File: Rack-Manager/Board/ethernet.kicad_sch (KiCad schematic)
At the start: 2 parts, among them J1 ARJM11C7-114-BA-EW2, U7 W6100Q

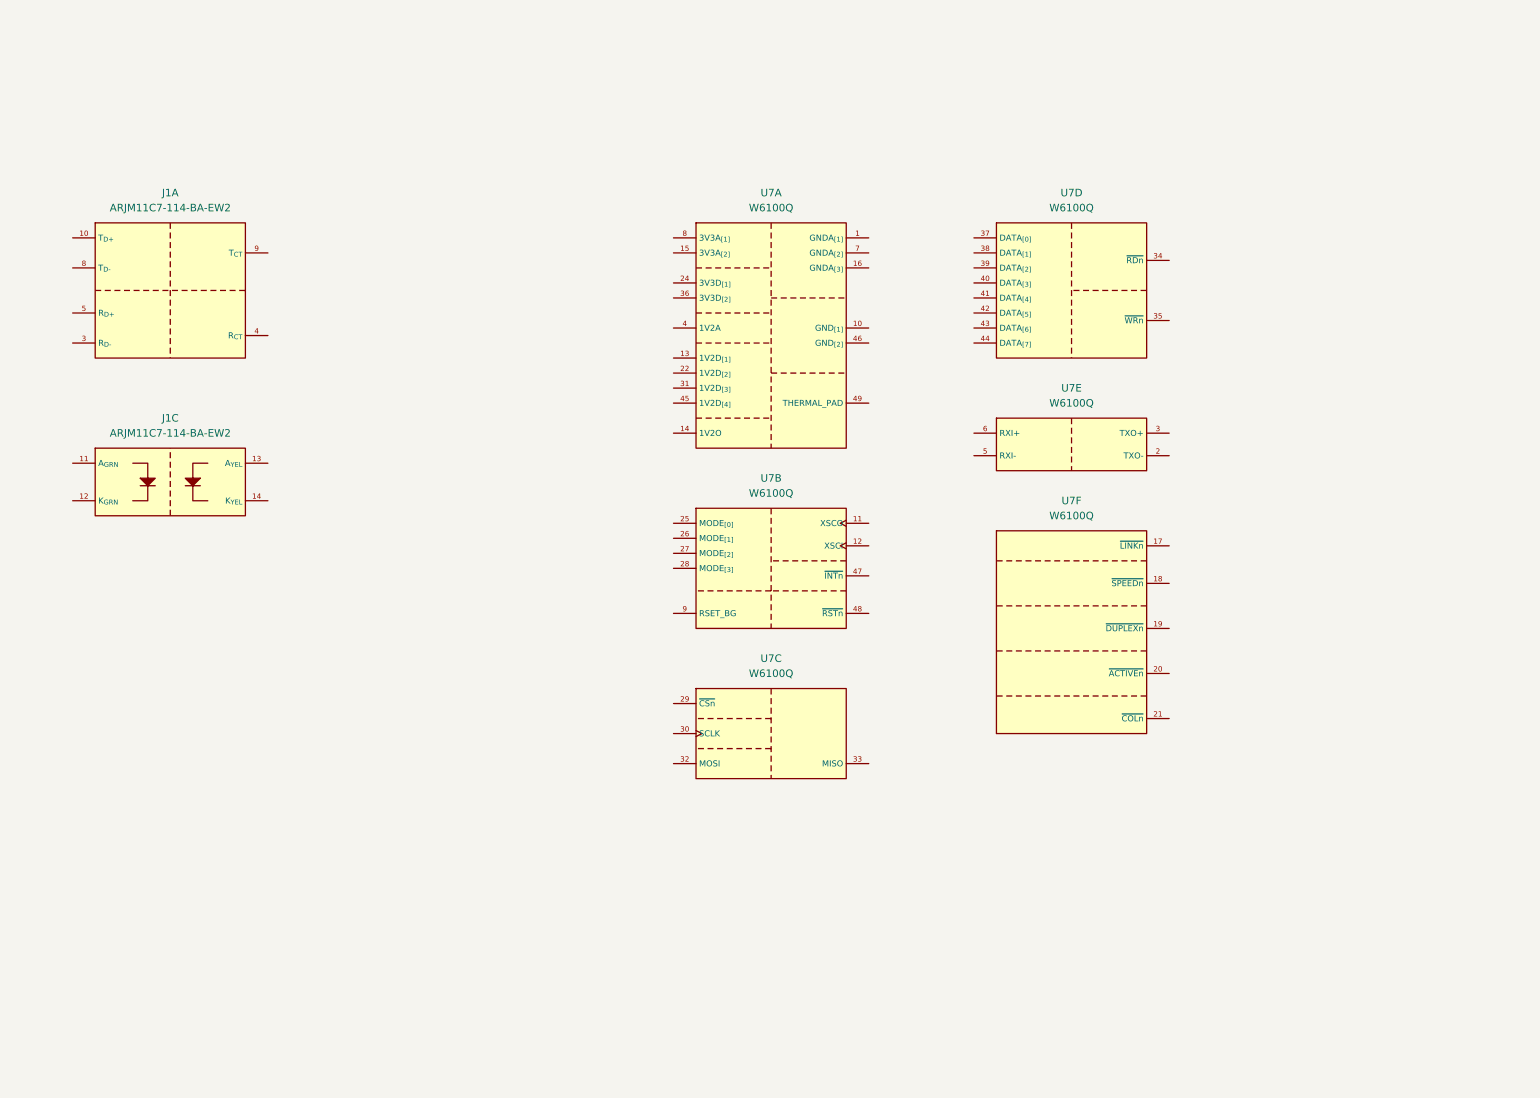
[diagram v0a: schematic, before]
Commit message: Updated Texas Instruments and WIZnet KiCAD libraries. Continued with the schematics design.
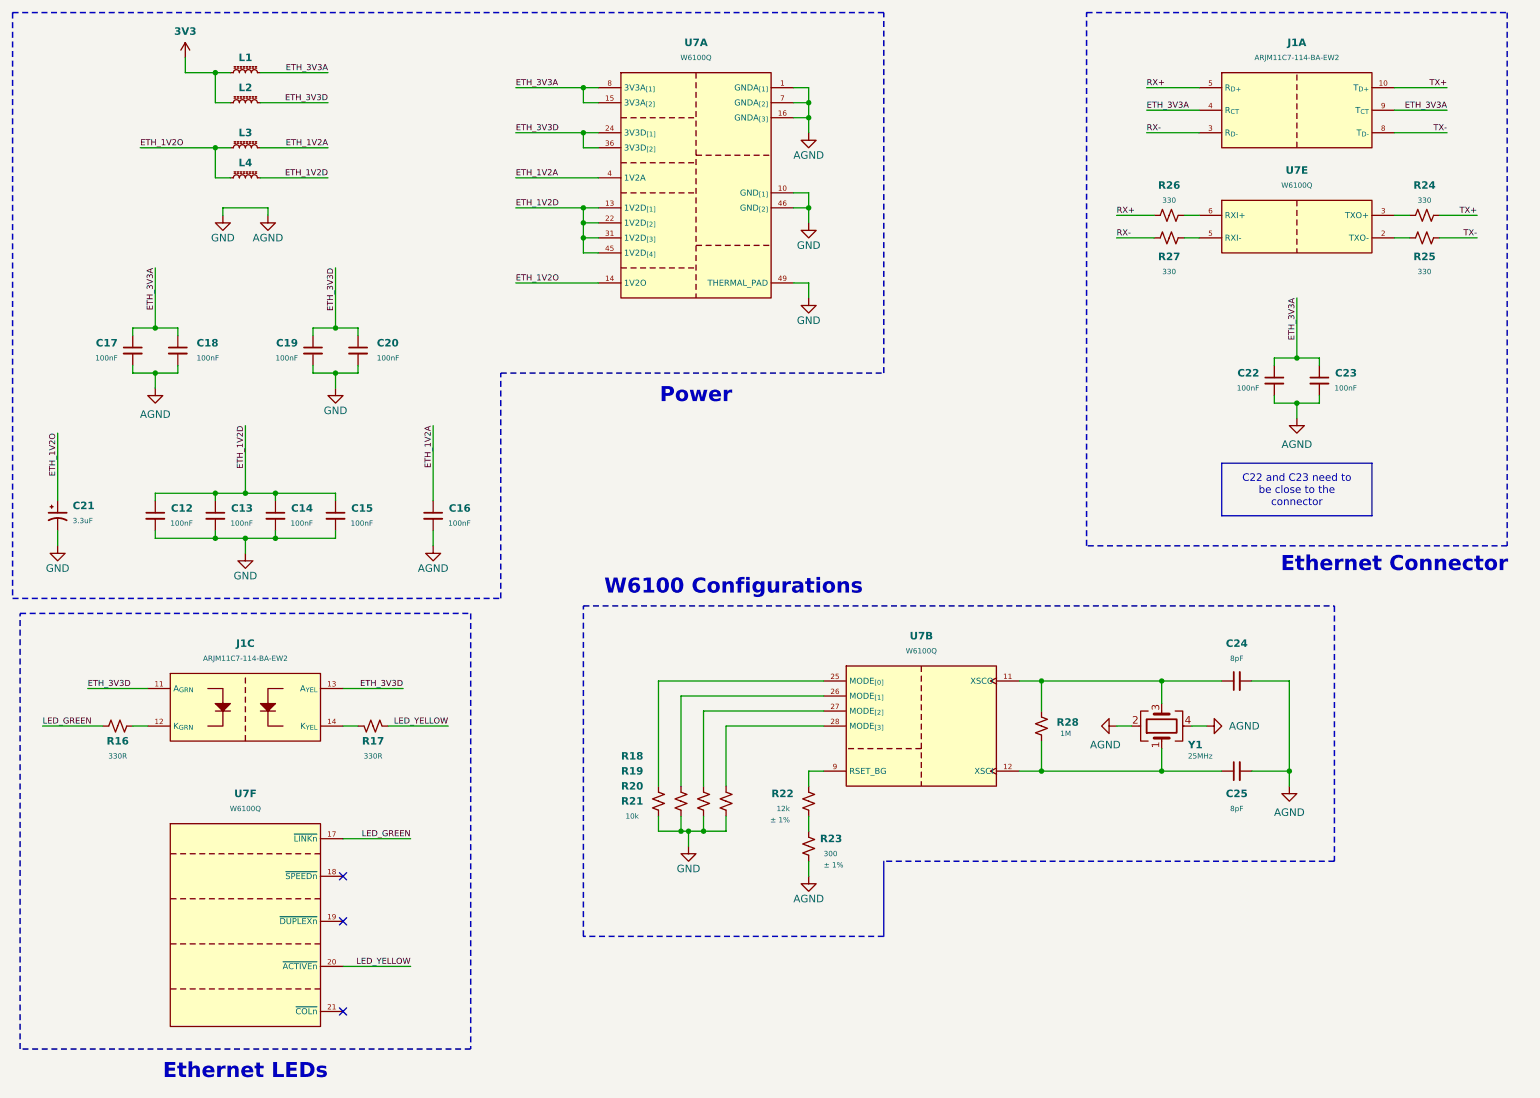
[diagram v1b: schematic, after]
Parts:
- removed unit 3 of U7
- removed unit 4 of U7
- added C12, C13, C14, C15, C16, C17, C18, C19, C20, C22, C23: 100nF, Capacitor_SMD:C_0402_1005Metric, symbol Device:C_Small
- added C21: 3.3uF, Capacitor_SMD:CP_Elec_4x5.7, symbol Device:C_Polarized_Small_US
- added C24, C25: 8pF, Capacitor_SMD:C_0402_1005Metric, symbol Device:C_Small
- added L1, L2, L3, L4: L_Ferrite_Small, symbol Device:L_Ferrite_Small
- added R16, R17: 330R, Resistor_SMD:R_0402_1005Metric, symbol Device:R_Small_US
- added R18, R19, R20, R21: 10k, Resistor_SMD:R_0402_1005Metric, symbol Device:R_Small_US
- added R22: 12k, Resistor_SMD:R_0402_1005Metric, symbol Device:R_Small_US
- added R23: 300, Resistor_SMD:R_0402_1005Metric, symbol Device:R_Small_US
- added R24, R25, R26, R27: 330, Resistor_SMD:R_0402_1005Metric, symbol Device:R_Small_US
- added R28: 1M, Resistor_SMD:R_0402_1005Metric, symbol Device:R_Small_US
- added Y1: 25MHz, symbol Device:Crystal_GND24
- U7: Manufacturer (none) -> WIZnet; Mouser Link (none) -> https://www.mouser.it/ProductDetail/950-W6100Q
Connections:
- net at U7.11 (XSCO): now also C24.1, R28.1, Y1.3
- net at U7.12 (XSCI): now also C25.1, R28.2, Y1.1
- net at U7.25 (MODE_{[0]}): now also R18.1
- net at U7.26 (MODE_{[1]}): now also R19.1
- net at U7.27 (MODE_{[2]}): now also R20.1
- net at U7.28 (MODE_{[3]}): now also R21.1
- net at U7.9 (RSET_BG): now also R22.1
- net TX+: now reaches J1.10 (T_{D+})
- net TX+: now also R24.1
- net RX-: now reaches J1.3 (R_{D-})
- net RX-: now also R27.2
- net ETH_3V3A: now reaches J1.4 (R_{CT})
- net ETH_3V3A: now also J1.9 (T_{CT}), U7.15 (3V3A_{[2]}), U7.8 (3V3A_{[1]}), C17.1, C18.1, C22.1, C23.1, L1.2
- net RX+: now reaches J1.5 (R_{D+})
- net RX+: now also R26.2
- net TX-: now reaches J1.8 (T_{D-})
- net TX-: now also R25.1
- net AGND: now reaches U7.1 (GNDA_{[1]})
- net AGND: now also U7.10 (GND_{[1]}), U7.16 (GNDA_{[3]}), U7.46 (GND_{[2]}), U7.49 (THERMAL_PAD), U7.7 (GNDA_{[2]}), C12.2, C13.2, C14.2, C15.2, C16.2, C17.2, C18.2, C19.2, C20.2, C21.2, C22.2, C23.2, C24.2, C25.2, R18.2, R19.2, R20.2, R21.2, R23.2, Y1.2, Y1.4
- net ETH_1V2D: now reaches U7.13 (1V2D_{[1]})
- net ETH_1V2D: now also U7.22 (1V2D_{[2]}), U7.31 (1V2D_{[3]}), U7.45 (1V2D_{[4]}), C12.1, C13.1, C14.1, C15.1, L4.2
- net ETH_1V2O: now reaches U7.14 (1V2O)
- net ETH_1V2O: now also C21.1, L3.1, L4.1
- net ETH_3V3D: now reaches U7.24 (3V3D_{[1]})
- net ETH_3V3D: now also J1.11 (A_{GRN}), J1.13 (A_{YEL}), U7.36 (3V3D_{[2]}), C19.1, C20.1, L2.2
- net ETH_1V2A: now reaches U7.4 (1V2A)
- net ETH_1V2A: now also C16.1, L3.2
- net at J1.12 (K_{GRN}): now also R16.1
- net at J1.14 (K_{YEL}): now also R17.1
- net at U7.2 (TXO-): now also R25.2
- net at U7.3 (TXO+): now also R24.2
- net at U7.5 (RXI-): now also R27.1
- net at U7.6 (RXI+): now also R26.1
- net LED_GREEN: now reaches U7.17 (~{LINKn})
- net LED_GREEN: now also R16.2
- net LED_YELLOW: now reaches U7.20 (~{ACTIVEn})
- net LED_YELLOW: now also R17.2
- new net: R22.2, R23.1
- new net 3V3: L1.1, L2.1
- no-connect marks 0 -> 3
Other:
- note added: "Ethernet Connector"
- note added: "Ethernet LEDs"
- note added: "Power"
- note added: "W6100 Configurations"
- title: Ethernet MAC+PHY -> Ethernet MAC+PHY and Connector
- moved on the sheet: J1C, U7A, U7E, U7F

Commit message: Updated Texas Instruments KiCAD library. Continued with the schematics design.
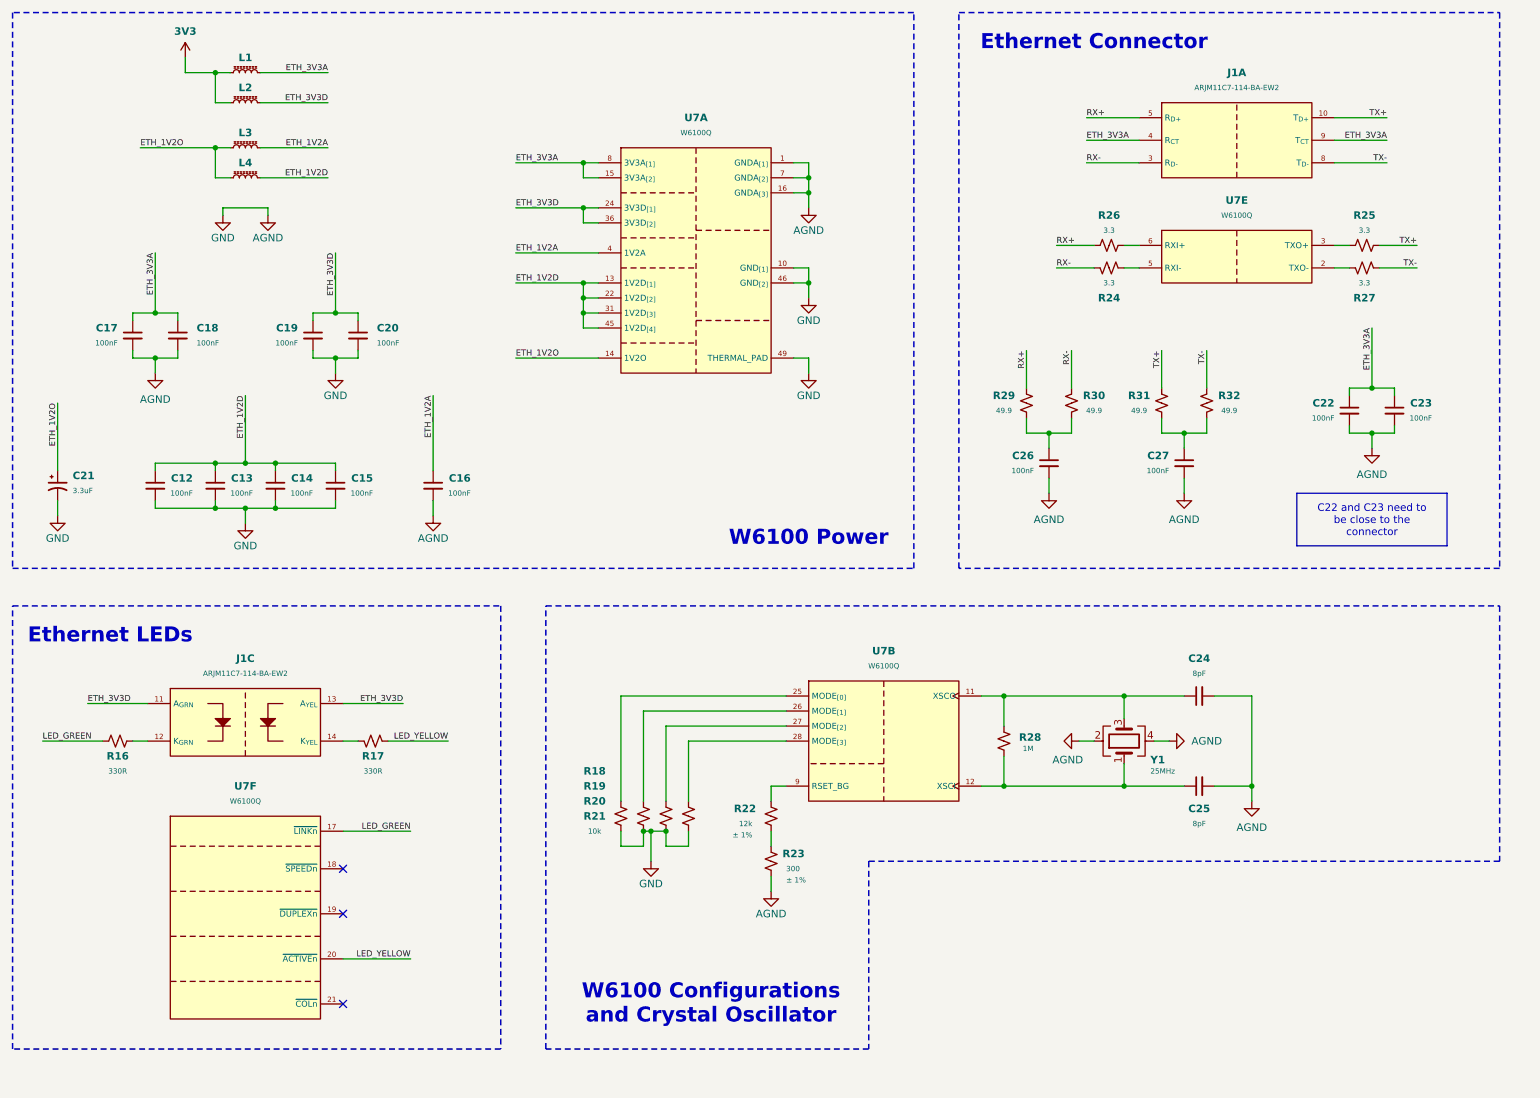
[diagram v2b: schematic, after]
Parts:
- added C26, C27: 100nF, Capacitor_SMD:C_0402_1005Metric, symbol Device:C_Small
- added R29, R30, R31, R32: 49.9, Resistor_SMD:R_0402_1005Metric, symbol Device:R_Small_US
- R24, R25, R26, R27: value 330 -> 3.3
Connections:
- net AGND: now also C26.2, C27.2
- net RX+: now also R29.1
- net RX-: now also R24.2, R30.1; no longer R27.2
- net TX+: now also R25.1, R31.1; no longer R24.1
- net TX-: now also R27.1, R32.1; no longer R25.1
- net at U7.5 (RXI-): now also R24.1; no longer R27.1
- net at U7.2 (TXO-): now also R27.2; no longer R25.2
- net at U7.3 (TXO+): now also R25.2; no longer R24.2
- new net: C27.1, R31.2, R32.2
- new net: C26.1, R29.2, R30.2
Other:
- note added: "W6100 Configurations and Crystal Oscillator"
- note added: "W6100 Power"
- note removed: "Power"
- note removed: "W6100 Configurations"
- moved on the sheet: C12, C13, C14, C15, C16, C17, C18, C19, C20, C21, C22, C23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

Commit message: Continued with the schematic drawing.
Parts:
- renumbered C17 to C14, C18 to C15, C19 to C16, C20 to C17, C21 to C18, C12 to C19, C13 to C20, C14 to C21, C15 to C22, C16 to C23, C26 to C24, C27 to C25, C22 to C26, C23 to C27, C24 to C28, C25 to C29
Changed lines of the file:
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@@
 		(on_board yes)
 		(dnp no)
-		(property "Reference" "C27"
+		(property "Reference" "C25"
 			(at 219.71 90.17 0)
 			(effects
@@
 			(project "Rack-Manager"
 				(path "/5d42174d-da49-4bca-870b-353868af7168/781970e2-2116-4faf-b2d3-2243f6c2f5bb"
-					(reference "C27")
+					(reference "C25")
 					(unit 1)
 				)
@@
 		(on_board yes)
 		(dnp no)
-		(property "Reference" "C25"
+		(property "Reference" "C29"
 			(at 224.79 149.86 90)
 			(effects
@@
 			(project "Rack-Manager"
 				(path "/5d42174d-da49-4bca-870b-353868af7168/781970e2-2116-4faf-b2d3-2243f6c2f5bb"
-					(reference "C25")
+					(reference "C29")
 					(unit 1)
 				)
@@
 		(on_board yes)
 		(dnp no)
-		(property "Reference" "C23"
+		(property "Reference" "C27"
 			(at 264.16 81.28 0)
 			(effects
@@
 			(project "Rack-Manager"
 				(path "/5d42174d-da49-4bca-870b-353868af7168/781970e2-2116-4faf-b2d3-2243f6c2f5bb"
-					(reference "C23")
+					(reference "C27")
 					(unit 1)
 				)
@@
 		(on_board yes)
 		(dnp no)
-		(property "Reference" "C22"
+		(property "Reference" "C26"
 			(at 247.65 81.28 0)
 			(effects
@@
 			(project "Rack-Manager"
 				(path "/5d42174d-da49-4bca-870b-353868af7168/781970e2-2116-4faf-b2d3-2243f6c2f5bb"
-					(reference "C22")
+					(reference "C26")
 					(unit 1)
 				)
@@
 		(dnp no)
 		(property "Reference" "R17"
-			(at 85.09 140.97 90)
+			(at 85.09 141.478 90)
 			(effects
 				(font
@@
 		)
 		(property "Value" "330R"
-			(at 85.09 143.51 90)
+			(at 85.09 144.018 90)
 			(effects
 				(font
@@
 		(on_board yes)
 		(dnp no)
-		(property "Reference" "C13"
+		(property "Reference" "C20"
 			(at 64.77 93.98 0)
 			(effects
@@
 			(project "Rack-Manager"
 				(path "/5d42174d-da49-4bca-870b-353868af7168/781970e2-2116-4faf-b2d3-2243f6c2f5bb"
-					(reference "C13")
+					(reference "C20")
 					(unit 1)
 				)
@@
 		(dnp no)
 		(property "Reference" "R16"
-			(at 41.91 140.97 90)
+			(at 41.91 141.478 90)
 			(effects
 				(font
@@
 		)
 		(property "Value" "330R"
-			(at 41.91 143.51 90)
+			(at 41.91 144.018 90)
 			(effects
 				(font
@@
 		(dnp no)
 		(fields_autoplaced yes)
-		(property "Reference" "C21"
-			(at 34.29 93.5481 0)
+		(property "Reference" "C18"
+			(at 34.29 93.5482 0)
 			(effects
 				(font
@@
 		)
 		(property "Value" "3.3uF"
-			(at 34.29 96.0881 0)
+			(at 34.29 96.0882 0)
 			(effects
 				(font
@@
 			(project "Rack-Manager"
 				(path "/5d42174d-da49-4bca-870b-353868af7168/781970e2-2116-4faf-b2d3-2243f6c2f5bb"
-					(reference "C21")
+					(reference "C18")
 					(unit 1)
 				)
@@
 		(on_board yes)
 		(dnp no)
-		(property "Reference" "C20"
+		(property "Reference" "C17"
 			(at 85.725 68.58 0)
 			(effects
@@
 			(project "Rack-Manager"
 				(path "/5d42174d-da49-4bca-870b-353868af7168/781970e2-2116-4faf-b2d3-2243f6c2f5bb"
-					(reference "C20")
+					(reference "C17")
 					(unit 1)
 				)
@@
 		(on_board yes)
 		(dnp no)
-		(property "Reference" "C19"
+		(property "Reference" "C16"
 			(at 72.39 68.58 0)
 			(effects
@@
 			(project "Rack-Manager"
 				(path "/5d42174d-da49-4bca-870b-353868af7168/781970e2-2116-4faf-b2d3-2243f6c2f5bb"
-					(reference "C19")
+					(reference "C16")
 					(unit 1)
 				)
@@
 		(on_board yes)
 		(dnp no)
-		(property "Reference" "C18"
+		(property "Reference" "C15"
 			(at 55.245 68.58 0)
 			(effects
@@
 			(project "Rack-Manager"
 				(path "/5d42174d-da49-4bca-870b-353868af7168/781970e2-2116-4faf-b2d3-2243f6c2f5bb"
-					(reference "C18")
+					(reference "C15")
 					(unit 1)
 				)
@@
 		(on_board yes)
 		(dnp no)
-		(property "Reference" "C15"
+		(property "Reference" "C22"
 			(at 85.09 93.98 0)
 			(effects
@@
 			(project "Rack-Manager"
 				(path "/5d42174d-da49-4bca-870b-353868af7168/781970e2-2116-4faf-b2d3-2243f6c2f5bb"
-					(reference "C15")
+					(reference "C22")
 					(unit 1)
 				)
@@
 		(on_board yes)
 		(dnp no)
-		(property "Reference" "C12"
+		(property "Reference" "C19"
 			(at 54.61 93.98 0)
 			(effects
@@
 			(project "Rack-Manager"
 				(path "/5d42174d-da49-4bca-870b-353868af7168/781970e2-2116-4faf-b2d3-2243f6c2f5bb"
-					(reference "C12")
+					(reference "C19")
 					(unit 1)
 				)
@@
 		(on_board yes)
 		(dnp no)
-		(property "Reference" "C26"
+		(property "Reference" "C24"
 			(at 196.85 90.17 0)
 			(effects
@@
 			(project "Rack-Manager"
 				(path "/5d42174d-da49-4bca-870b-353868af7168/781970e2-2116-4faf-b2d3-2243f6c2f5bb"
-					(reference "C26")
+					(reference "C24")
 					(unit 1)
 				)
@@
 		(on_board yes)
 		(dnp no)
-		(property "Reference" "C17"
+		(property "Reference" "C14"
 			(at 41.91 68.58 0)
 			(effects
@@
 			(project "Rack-Manager"
 				(path "/5d42174d-da49-4bca-870b-353868af7168/781970e2-2116-4faf-b2d3-2243f6c2f5bb"
-					(reference "C17")
+					(reference "C14")
 					(unit 1)
 				)
@@
 		(on_board yes)
 		(dnp no)
-		(property "Reference" "C24"
+		(property "Reference" "C28"
 			(at 224.79 124.46 90)
 			(effects
@@
 			(project "Rack-Manager"
 				(path "/5d42174d-da49-4bca-870b-353868af7168/781970e2-2116-4faf-b2d3-2243f6c2f5bb"
-					(reference "C24")
+					(reference "C28")
 					(unit 1)
 				)
@@
 		(on_board yes)
 		(dnp no)
-		(property "Reference" "C14"
+		(property "Reference" "C21"
 			(at 74.93 93.98 0)
 			(effects
@@
 			(project "Rack-Manager"
 				(path "/5d42174d-da49-4bca-870b-353868af7168/781970e2-2116-4faf-b2d3-2243f6c2f5bb"
-					(reference "C14")
+					(reference "C21")
 					(unit 1)
 				)
@@
 		(on_board yes)
 		(dnp no)
-		(property "Reference" "C16"
+		(property "Reference" "C23"
 			(at 101.6 93.98 0)
 			(effects
@@
 			(project "Rack-Manager"
 				(path "/5d42174d-da49-4bca-870b-353868af7168/781970e2-2116-4faf-b2d3-2243f6c2f5bb"
-					(reference "C16")
+					(reference "C23")
 					(unit 1)
 				)
